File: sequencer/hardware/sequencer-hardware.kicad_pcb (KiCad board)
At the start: 4 copper layers, 100.6 x 151.4 mm, 135 parts, among them J1 Barrel Jack, J10 JST_4-pin_male, J11 Conn_01x03, J12 Conn_01x03, J13 Conn_01x03, J14 Conn_01x03, J15 JST_4-pin_male, J16 JST_4-pin_male, J17 Conn_01x03, J2 40Pin 0.1"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

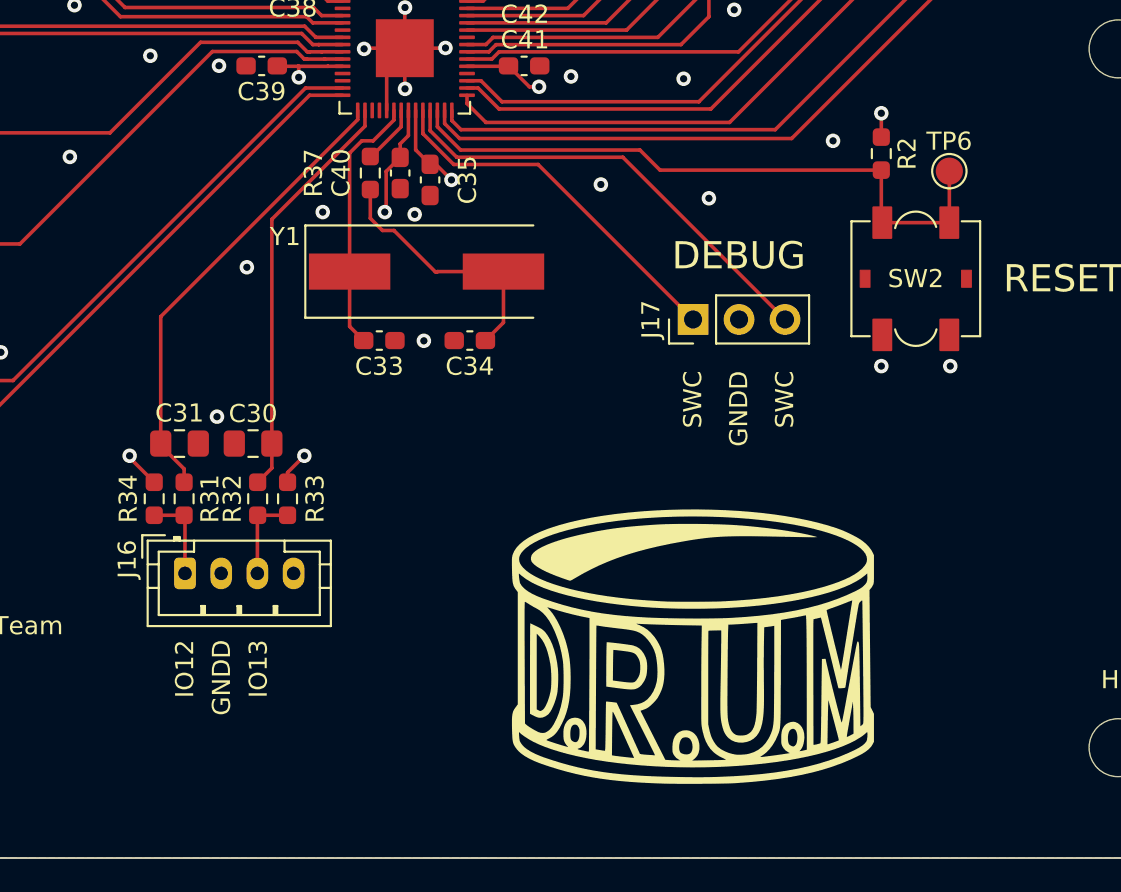
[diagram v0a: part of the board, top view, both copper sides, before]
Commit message: Add OLED header
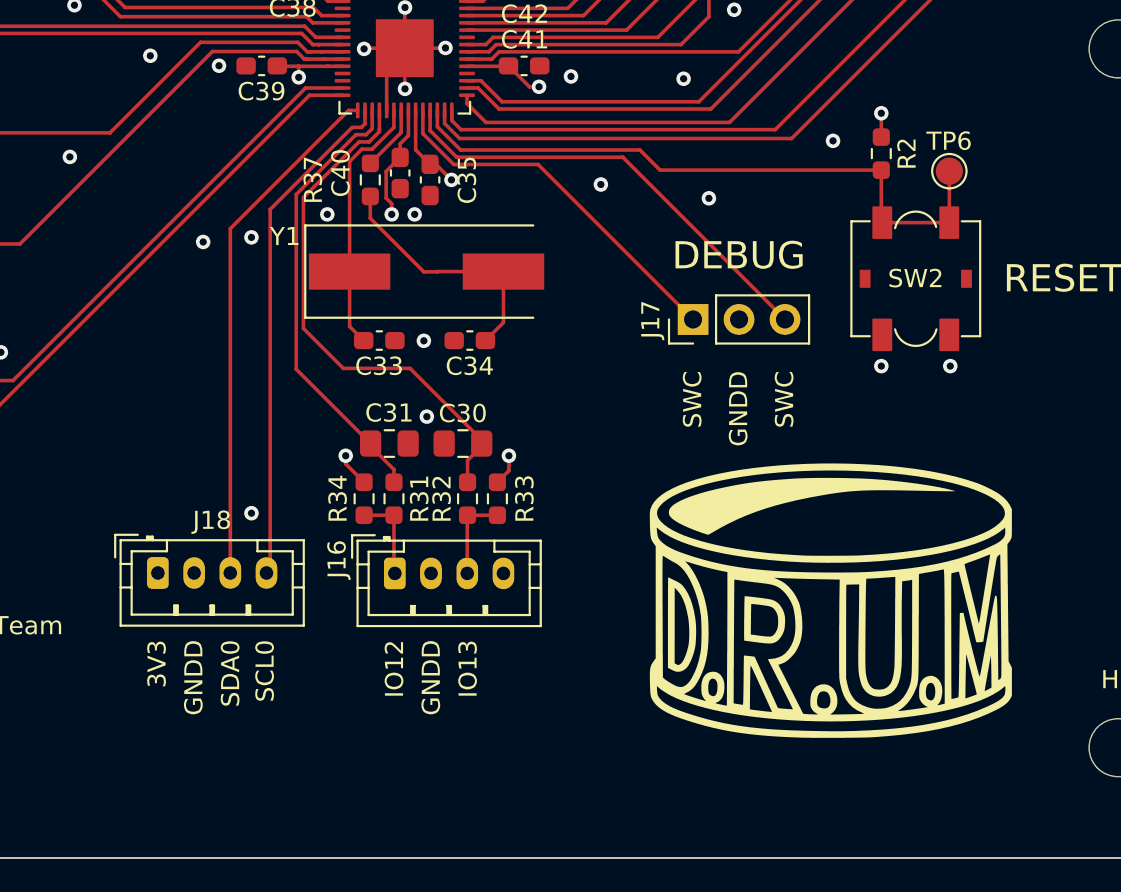
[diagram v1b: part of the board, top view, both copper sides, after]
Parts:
- added J18: JST_4-pin_male, Connector_JST:JST_PH_B4B-PH-K_1x04_P2.00mm_Vertical, F.Cu at (67.0, 161.0)
- moved J16 11.6 mm to (80.1, 161.1)
- moved C30 11.6 mm to (83.8, 153.9)
- moved C31 11.6 mm to (79.8, 153.9)
- moved R31 11.6 mm to (80.0, 156.9)
- moved R32 11.6 mm to (84.1, 156.9)
- moved R33 11.6 mm to (85.7, 156.9)
- moved R34 11.6 mm to (78.4, 156.9)
- moved G*** 8.03 mm to (104.1, 162.6)
- moved R37 0.38 mm to (78.7, 139.3)
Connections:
- C30 pad 1: /D.R.U.M. Sequencer Digital/GPIO13_ENC31 -> /D.R.U.M. Sequencer Digital/GPIO15_ENC31
- C31 pad 1: /D.R.U.M. Sequencer Digital/GPIO12_ENC30 -> /D.R.U.M. Sequencer Digital/GPIO14_ENC30
- R31 pad 1: /D.R.U.M. Sequencer Digital/GPIO12_ENC30 -> /D.R.U.M. Sequencer Digital/GPIO14_ENC30
- R32 pad 1: /D.R.U.M. Sequencer Digital/GPIO13_ENC31 -> /D.R.U.M. Sequencer Digital/GPIO15_ENC31
- U8 pad 15: /D.R.U.M. Sequencer Digital/GPIO12_ENC30 -> /D.R.U.M. Sequencer Digital/GPIO12_SDA0
- U8 pad 16: /D.R.U.M. Sequencer Digital/GPIO13_ENC31 -> /D.R.U.M. Sequencer Digital/GPIO13_SCL0
- U8 pad 17: unconnected-(U8-Pad17) -> /D.R.U.M. Sequencer Digital/GPIO14_ENC30
- U8 pad 18: unconnected-(U8-Pad18) -> /D.R.U.M. Sequencer Digital/GPIO15_ENC31
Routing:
- net /D.R.U.M. Sequencer Digital/GPIO15_ENC31: track 0.00 -> 29.2 mm
- net /D.R.U.M. Sequencer Digital/GPIO12_SDA0: track 0.00 -> 28.8 mm
- net /D.R.U.M. Sequencer Digital/GPIO13_SCL0: track 0.00 -> 28.1 mm
- net /D.R.U.M. Sequencer Digital/GPIO12_ENC30: track 25.6 -> 0.00 mm
- net /D.R.U.M. Sequencer Digital/GPIO14_ENC30: track 0.00 -> 24.8 mm
- net /D.R.U.M. Sequencer Digital/GPIO13_ENC31: track 23.0 -> 0.00 mm
- net GNDD: vias 84 -> 86
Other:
- board text added: "SCL0"
- board text added: "SDA0"

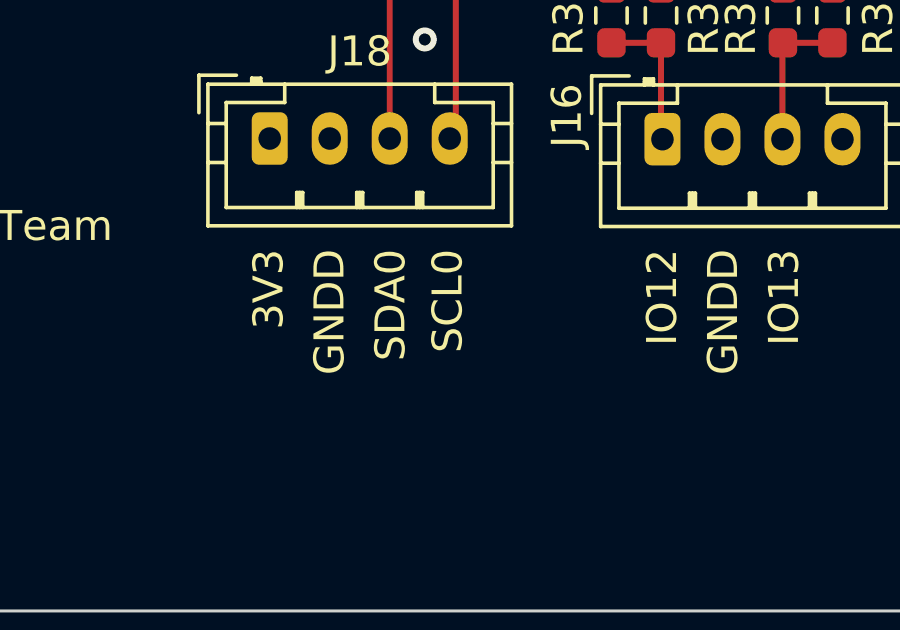
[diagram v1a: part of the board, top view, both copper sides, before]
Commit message: Increase size of layer 3 planes
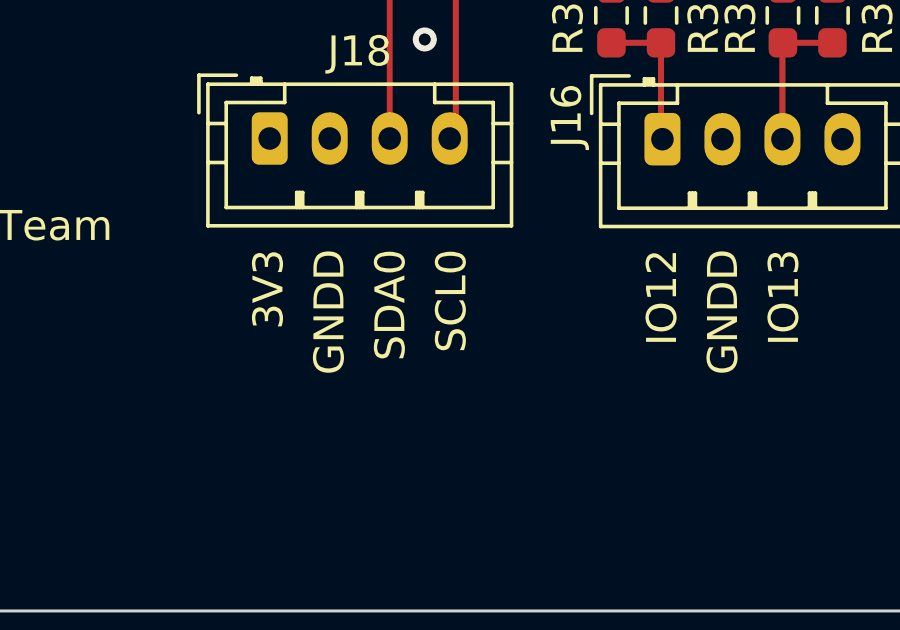
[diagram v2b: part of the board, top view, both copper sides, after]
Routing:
- added copper zone on In2.Cu, net +9V
- added copper zone on In2.Cu, net -5V
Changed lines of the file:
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@@
     (effects (font (size 1 1) (thickness 0.150084)) (justify right))
   )
-  (gr_text "SCL0" (at 72.898 164.719 90) (layer "F.SilkS")
+  (gr_text "SCL0" (at 73.025 164.719 90) (layer "F.SilkS")
     (effects (font (size 1 1) (thickness 0.150084)) (justify right))
   )
@@
         (xy 121.0174 102.300032)
         (xy 125.9704 102.300032)
-        (xy 125.9704 127.446032)
-        (xy 91.948 127.446032)
-        (xy 42.4044 77.851)
-        (xy 42.4044 60.898032)
+        (xy 125.984 176.784)
+        (xy 25.4 176.784)
+        (xy 25.3864 77.851)
+        (xy 25.3864 60.898032)
         (xy 75.1704 60.898032)
+      )
+    )
+  )
+  (zone (net 90) (net_name "+9V") (layer "In2.Cu") (hatch edge 0.508)
+    (priority 1)
+    (connect_pads yes (clearance 0.508))
+    (min_thickness 0.254) (filled_areas_thickness no)
+    (fill yes (thermal_gap 0.508) (thermal_bridge_width 0.508))
+    (polygon
+      (pts
+        (xy 69.469 60.071)
+        (xy 25.4 60.071)
+        (xy 25.4 25.4)
+        (xy 69.469 25.4)
       )
     )
@@
       )
     )
+  )
+  (zone (net 81) (net_name "-5V") (layer "In2.Cu") (hatch edge 0.508)
+    (connect_pads yes (clearance 0.508))
+    (min_thickness 0.254) (filled_areas_thickness no)
+    (fill yes (thermal_gap 0.508) (thermal_bridge_width 0.508))
+    (polygon
+      (pts
+        (xy 125.984 101.6)
+        (xy 120.777 101.6)
+        (xy 118.237 104.14)
+        (xy 110.49 104.14)
+        (xy 105.537 99.06)
+        (xy 105.537 82.296)
+        (xy 98.806 75.565)
+        (xy 91.186 75.565)
+        (xy 75.692 60.071)
+        (xy 70.231 60.071)
+        (xy 70.231 25.4)
+        (xy 125.984 25.4)
+      )
+    )

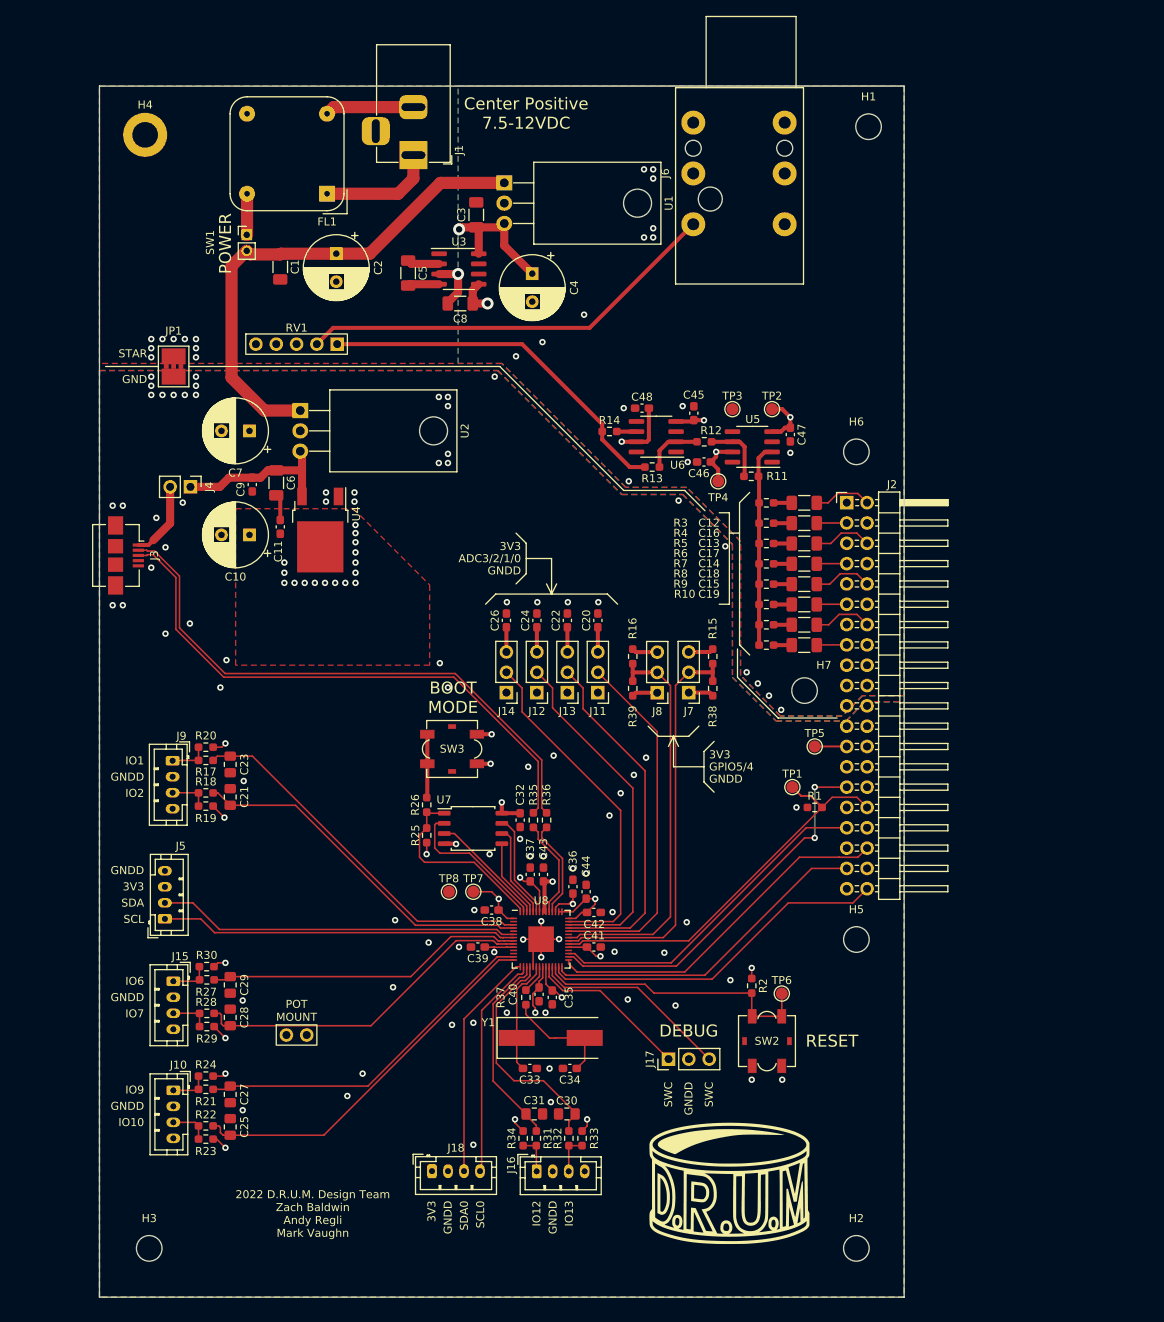
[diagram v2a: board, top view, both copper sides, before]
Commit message: Resize sequencer PCB
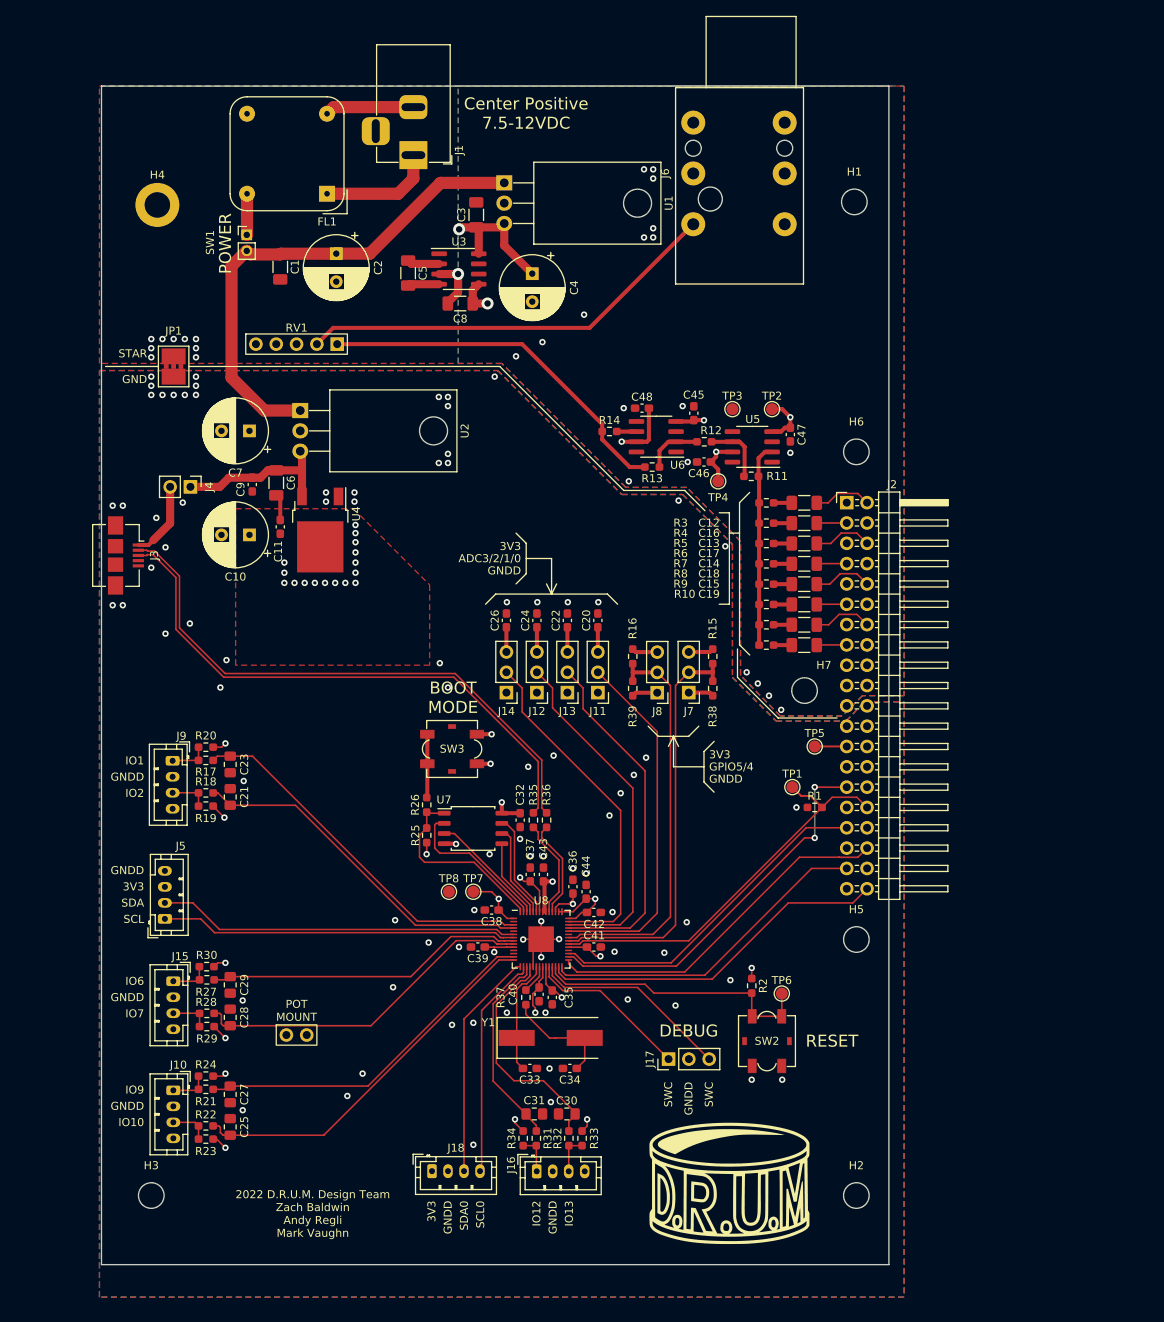
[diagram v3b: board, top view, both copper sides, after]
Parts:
- moved H1 9.56 mm to (119.8, 39.9)
- moved H4 8.89 mm to (32.6, 40.3)
- moved H3 6.61 mm to (31.9, 164.1)
- moved H2 6.60 mm to (120.0, 164.1)
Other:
- board size 100.6 x 151.4 mm -> 98.4 x 147.3 mm
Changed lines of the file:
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@@
   )
   (footprint "MountingHole:MountingHole_3.2mm_M3_ISO14580_Pad" (layer "F.Cu")
-    (at 31.1125 31.496)
+    (at 32.639 40.259)
     (descr "Mounting Hole 3.2mm, M3, ISO14580")
     (tags "mounting hole 3.2mm m3 iso14580")
@@
   )
   (footprint "MountingHole:MountingHole_3.2mm_M3_ISO14580" locked (layer "F.Cu")
-    (at 121.5365 30.48)
+    (at 119.761 39.878)
     (descr "Mounting Hole 3.2mm, no annular, M3, ISO14580")
     (tags "mounting hole 3.2mm no annular m3 iso14580")
@@
   )
   (footprint "MountingHole:MountingHole_3.2mm_M3_ISO14580" locked (layer "F.Cu")
-    (at 31.6205 170.688)
+    (at 31.877 164.084)
     (descr "Mounting Hole 3.2mm, no annular, M3, ISO14580")
     (tags "mounting hole 3.2mm no annular m3 iso14580")
@@
   )
   (footprint "MountingHole:MountingHole_3.2mm_M3_ISO14580" locked (layer "F.Cu")
-    (at 120.0125 170.688)
+    (at 120.0125 164.084)
     (descr "Mounting Hole 3.2mm, no annular, M3, ISO14580")
     (tags "mounting hole 3.2mm no annular m3 iso14580")
@@
   (gr_poly
     (pts
-      (xy 25.4 25.4)
-      (xy 125.984 25.4)
-      (xy 125.984 176.784)
-      (xy 25.4 176.784)
+      (xy 25.654 25.4)
+      (xy 124.079 25.4)
+      (xy 124.079 172.72)
+      (xy 25.654 172.72)
     ) (layer "Edge.Cuts") (width 0.1) (fill none))
   (gr_text "D.R.U.M.\nSequencer\nHW Design REV: 1.0\nLayout REV: A\nOrder No.    \nP/N DRUM-SQ-1000" (at 52.07 166.37) (layer "B.SilkS")

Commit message: Add board notches; align mounting holes
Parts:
- moved JP1 16.7 mm to (18.2, 57.7)
- moved U2 11.2 mm to (39.4, 64.4)
- moved C7 10.5 mm to (33.7, 68.1)
- moved H4 8.53 mm to (32.0, 31.8)
- moved H2 4.19 mm to (119.0, 160.0)
- moved H3 2.29 mm to (32.0, 166.4)
- moved H1 1.93 mm to (119.0, 38.1)
- moved H5 1.02 mm to (119.0, 132.1)
- moved H6 1.02 mm to (119.0, 71.1)
- moved SW1 0.36 mm to (43.8, 44.4)
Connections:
- RV1 pad 1: Net-(R13-Pad2) -> GNDA
- RV1 pad 2: Net-(J6-PadT) -> Net-(R13-Pad2)
- RV1 pad 4: (no net) -> Net-(J6-PadT)
- RV1 pad 5: (no net) -> GNDA
- RV1 pad 6: (no net) -> unconnected-(RV1-Pad6)
- RV1 pad 7: (no net) -> unconnected-(RV1-Pad7)
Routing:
- net +9V: track 63.0 -> 55.8 mm
- net Net-(J6-PadT): track 53.3 -> 59.0 mm
- net Net-(R13-Pad2): track 45.9 -> 50.1 mm
- net GNDA: track 6.60 -> 10.5 mm, vias 28 -> 36
- net +5VD: track 24.7 -> 26.1 mm
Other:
- outline, holes or cut-outs redrawn
- board text removed: "STAR GND"
